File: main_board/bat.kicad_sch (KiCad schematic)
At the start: 44 parts, among them IC1 MP2722GRH-0000-Z, IC2 MP3429GL-Z, IC3 NX3DV42GU, IC4 AP2204R-3.3TRG1, J4 USB_B_Micro, J5 USB_C_Receptacle_USB2.0, U3 ATmega32U4-M, Y1 Crystal

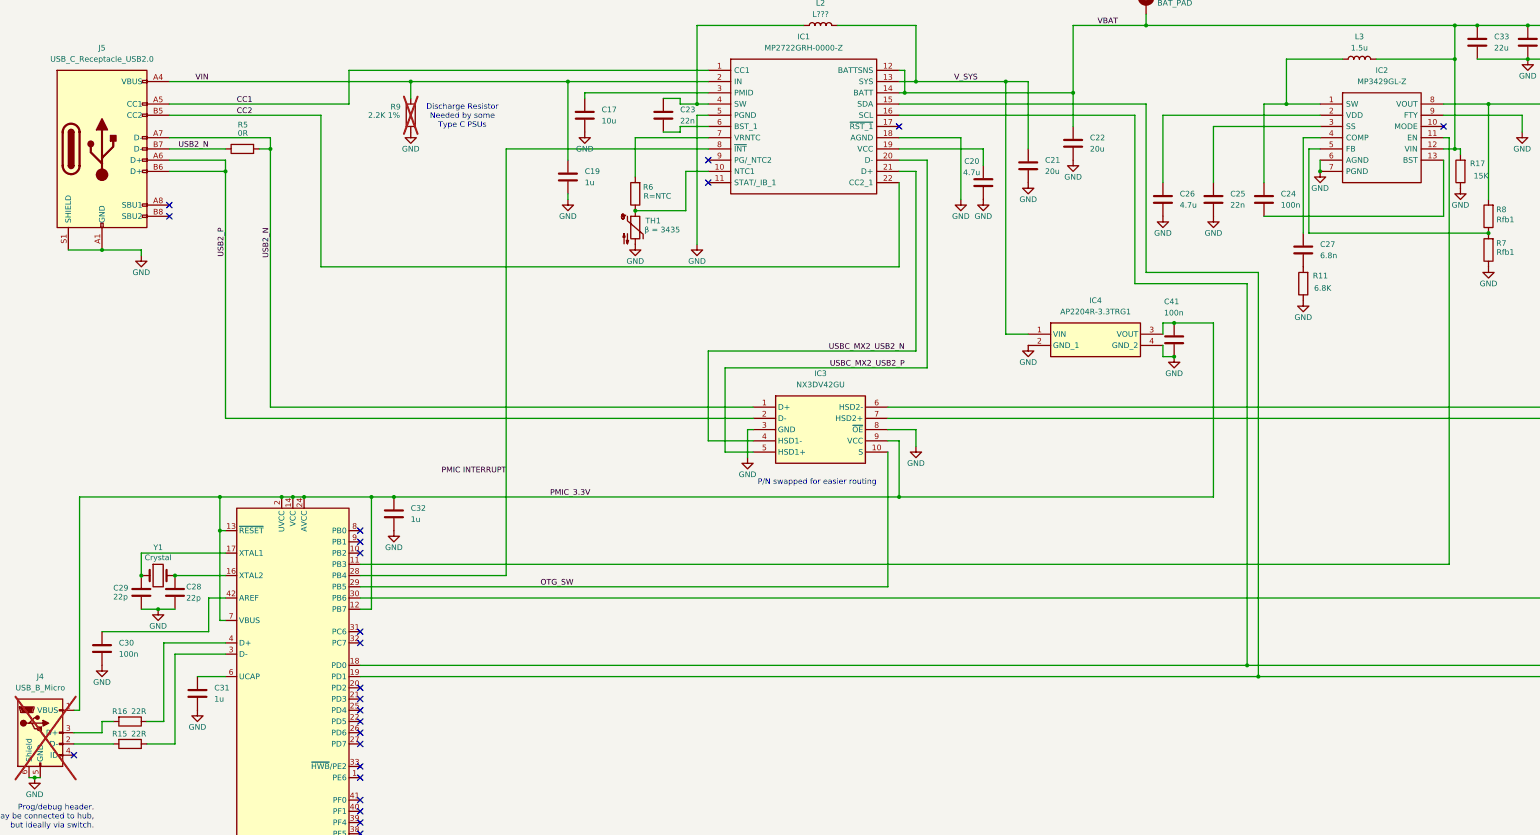
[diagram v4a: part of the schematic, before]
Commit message: Bunch more routing, mainly added MIPI interface, reworked power management a bit
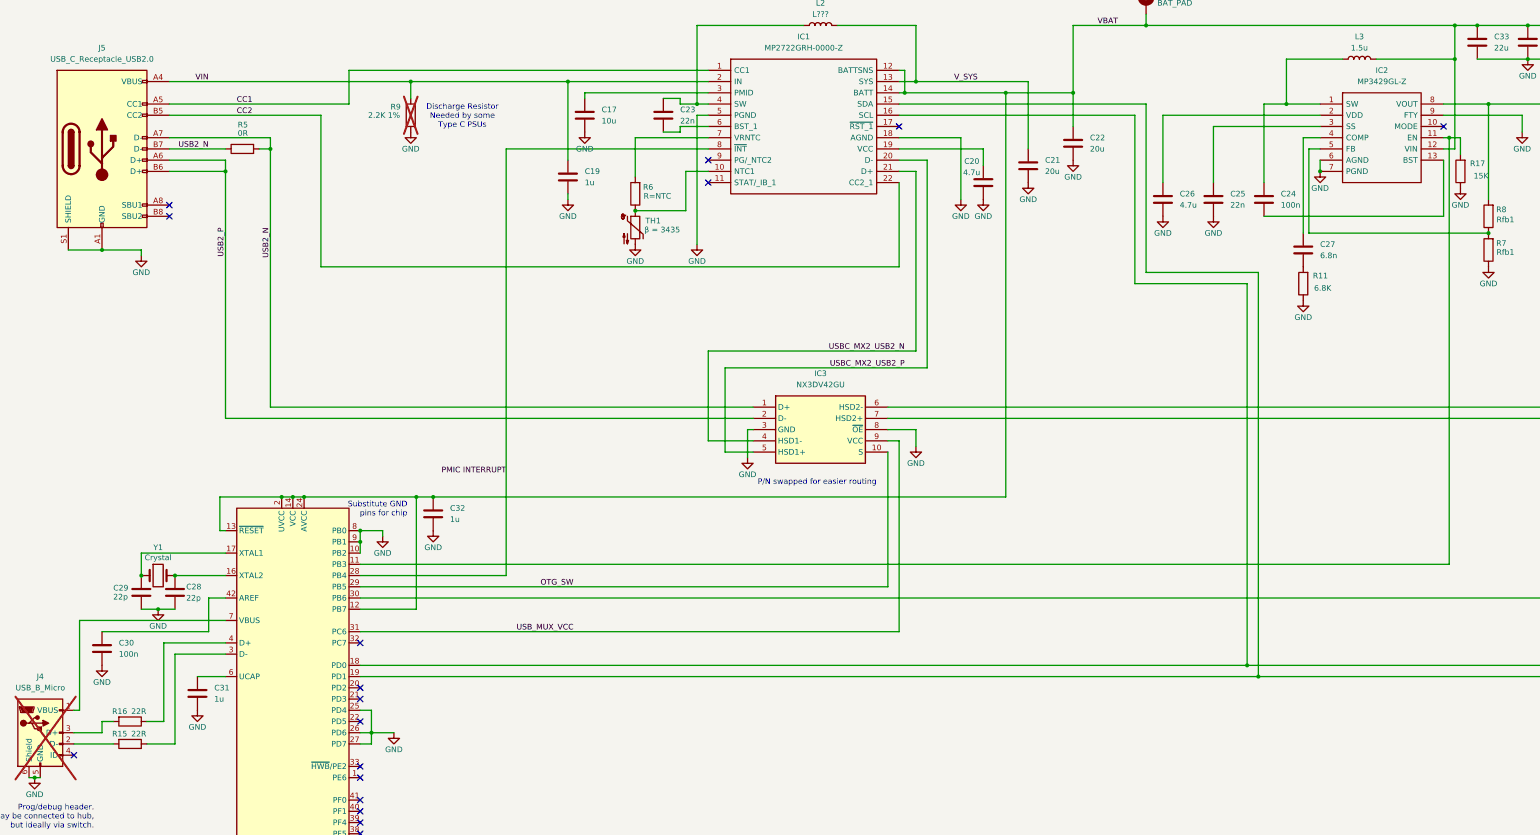
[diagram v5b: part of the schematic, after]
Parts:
- removed C41: 100n, Capacitor_SMD:C_0805_2012Metric_Pad1.18x1.45mm_HandSolder, symbol Device:C
- removed IC4: AP2204R-3.3TRG1, AP2204R33TRG1, symbol 000_Custom:AP2204R-3.3TRG1
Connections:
- net GND: now also U3.10 (PB2), U3.25 (PD4), U3.26 (PD6), U3.27 (PD7), U3.8 (PB0), U3.9 (PB1)
- net VBAT: now also C32.2, U3.12 (PB7), U3.13 (~{RESET}), U3.14 (VCC), U3.2 (UVCC), U3.24 (AVCC), U3.34 (VCC), U3.44 (AVCC); no longer R17.2
- net at IC2.11 (EN), U3.11 (PB3): now also R17.2
- net USB_MUX_VCC: now reaches U3.31 (PC6)
- net USB_MUX_VCC: now also IC3.9 (VCC)
- removed net PMIC_3.3V: C32.2, IC3.9 (VCC), J4.1 (VBUS), U3.12 (PB7), U3.13 (~{RESET}), U3.14 (VCC), U3.2 (UVCC), U3.24 (AVCC), U3.34 (VCC), U3.44 (AVCC), U3.7 (VBUS)
- new net: J4.1 (VBUS), U3.7 (VBUS)
- no-connect marks 26 -> 19
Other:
- note added: "Substitute GND pins for chip"
- moved on the sheet: C32

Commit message: Bunch of fixes + audio out interface
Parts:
- added C41: 100n, Capacitor_SMD:C_0805_2012Metric_Pad1.18x1.45mm_HandSolder, symbol Device:C
- added R26: 430K, Resistor_SMD:R_0805_2012Metric_Pad1.20x1.40mm_HandSolder, symbol Device:R
- added U5: AP2204RB-3.3, Package_TO_SOT_SMD:SOT-89-3, symbol Regulator_Linear:AP2204RB-3.3
- C20, C26: value 4.7u -> 10u
- C25: value 22n -> 100n
- C27: value 6.8n -> 10n
- C30: value 100n -> 1u
- L2: value L??? -> 4.7u
- R7: value Rfb1 -> 100K
- R8: value Rfb1 -> 33K
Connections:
- net +5V: now also R26.2; no longer R8.2
- net GND: now also U3.11 (PB3), U3.12 (PB7), C41.1, U5.2 (GND)
- net VBAT: no longer C32.2, U3.12 (PB7), U3.13 (~{RESET}), U3.14 (VCC), U3.2 (UVCC), U3.24 (AVCC), U3.34 (VCC), U3.44 (AVCC)
- net V_SYS: now also U5.3 (VIN)
- net BOOST_EN: now reaches IC2.11 (EN), R17.2
- net BOOST_EN: now also U3.1 (PE6); no longer U3.11 (PB3)
- net at J4.1 (VBUS), U3.7 (VBUS): now also U3.2 (UVCC)
- net 3.3v: now reaches U3.41 (PF0)
- net CM5_PMIC_EN renamed USB_SW_VCC
- net USB_SW_VCC: now also IC3.9 (VCC)
- net USB_MUX_VCC: no longer names the net of U3.31 (PC6)
- net USB_MUX_VCC: no longer IC3.9 (VCC)
- new net: R26.1, R8.2
- new net PMIC_3.3V: C32.2, C41.2, U3.13 (~{RESET}), U3.14 (VCC), U3.24 (AVCC), U3.34 (VCC), U3.44 (AVCC), U5.1 (VOUT)
- no-connect marks 19 -> 7

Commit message: Implement power monitoring
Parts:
- removed H9: BAT_PAD, TestPoint:TestPoint_Pad_4.0x4.0mm, symbol Mechanical:MountingHole_Pad_MP
- added BT1: Battery_Cell, 000_custom:Bat_terminal, symbol Device:Battery_Cell
- added C64: 100n, Capacitor_SMD:C_0805_2012Metric_Pad1.18x1.45mm_HandSolder, symbol Device:C
- added R41: 0.01R, Resistor_SMD:R_1206_3216Metric_Pad1.30x1.75mm_HandSolder, symbol Device:R
- added R42, R43: 10R, Resistor_SMD:R_0805_2012Metric_Pad1.20x1.40mm_HandSolder, symbol Device:R
- added U7: INA220AIDGST, DGS10, symbol 000_Custom:INA220AIDGST
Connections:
- net GND: now also BT1.2 (-), U7.1 (A1), U7.2 (A0), U7.7 (GND)
- net IIC_SCL: now also U7.5 (SCL)
- net IIC_SDA: now also U7.4 (SDA)
- net PMIC_3.3V: now also U7.6 (VS)
- net VBAT: now also R41.2, R43.2, U7.8 (VBUS)
- new net: BT1.1 (+), R41.1, R42.2
- new net: C64.1, R42.1, U7.9 (VIN-)
- new net: C64.2, R43.1, U7.10 (VIN+)
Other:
- moved on the sheet: C17, C19, C20, C21, C22, C23, C24, C25, C26, C27, C28, C29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

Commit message: Add expansion slot
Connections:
- net GND: no longer U7.1 (A1), U7.2 (A0)
- net IIC_SDA: now also U7.1 (A1), U7.2 (A0)
- net USBC_MX2_USB2_N: now also IC1.20 (D-), IC3.5 (HSD1+); no longer IC1.21 (D+), IC3.4 (HSD1-)
- net USBC_MX2_USB2_P: now also IC1.21 (D+), IC3.4 (HSD1-); no longer IC1.20 (D-), IC3.5 (HSD1+)
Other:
- moved on the sheet: R43
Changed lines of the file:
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@@
 	)
 	(junction
-		(at 358.14 54.61)
-		(diameter 0)
-		(color 0 0 0 0)
-	)
-	(junction
 		(at 163.83 115.57)
 		(diameter 0)
@@
 	)
 	(junction
+		(at 262.89 57.15)
+		(diameter 0)
+		(color 0 0 0 0)
+	)
+	(junction
 		(at 262.89 49.53)
 		(diameter 0)
@@
 	)
 	(junction
+		(at 358.14 52.07)
+		(diameter 0)
+		(color 0 0 0 0)
+	)
+	(junction
 		(at 227.33 86.36)
 		(diameter 0)
@@
 	)
 	(junction
-		(at 262.89 55.88)
+		(at 361.95 46.99)
 		(diameter 0)
 		(color 0 0 0 0)
@@
 	(wire
 		(pts
-			(xy 284.48 55.88) (xy 284.48 54.61)
-		)
-		(stroke
-			(width 0)
-			(type default)
-		)
-	)
-	(wire
-		(pts
 			(xy 318.77 99.06) (xy 314.96 99.06)
 		)
@@
 	(wire
 		(pts
-			(xy 262.89 55.88) (xy 267.97 55.88)
+			(xy 262.89 57.15) (xy 269.24 57.15)
 		)
 		(stroke
@@
 	(wire
 		(pts
+			(xy 262.89 49.53) (xy 262.89 57.15)
+		)
+		(stroke
+			(width 0)
+			(type default)
+		)
+	)
+	(wire
+		(pts
 			(xy 58.42 86.36) (xy 113.03 86.36)
 		)
@@
 	(wire
 		(pts
+			(xy 361.95 52.07) (xy 361.95 46.99)
+		)
+		(stroke
+			(width 0)
+			(type default)
+		)
+	)
+	(wire
+		(pts
 			(xy 284.48 29.21) (xy 274.32 29.21)
 		)
@@
 	(wire
 		(pts
-			(xy 220.98 160.02) (xy 381 160.02)
+			(xy 358.14 52.07) (xy 358.14 54.61)
 		)
 		(stroke
@@
 	(wire
 		(pts
-			(xy 86.36 180.34) (xy 88.9 180.34)
+			(xy 220.98 160.02) (xy 381 160.02)
 		)
 		(stroke
@@
 	(wire
 		(pts
-			(xy 43.18 231.14) (xy 45.72 231.14)
+			(xy 86.36 180.34) (xy 88.9 180.34)
 		)
 		(stroke
@@
 	(wire
 		(pts
-			(xy 314.96 99.06) (xy 314.96 120.65)
+			(xy 43.18 231.14) (xy 45.72 231.14)
 		)
 		(stroke
@@
 	(wire
 		(pts
-			(xy 101.6 203.2) (xy 224.79 203.2)
+			(xy 314.96 99.06) (xy 314.96 120.65)
 		)
 		(stroke
@@
 	(wire
 		(pts
-			(xy 134.62 101.6) (xy 134.62 198.12)
+			(xy 101.6 203.2) (xy 224.79 203.2)
 		)
 		(stroke
@@
 	(wire
 		(pts
-			(xy 358.14 54.61) (xy 358.14 58.42)
+			(xy 134.62 101.6) (xy 134.62 198.12)
 		)
 		(stroke
@@
 	(wire
 		(pts
+			(xy 361.95 46.99) (xy 403.86 46.99)
+		)
+		(stroke
+			(width 0)
+			(type default)
+		)
+	)
+	(wire
+		(pts
 			(xy 372.11 106.68) (xy 378.46 106.68)
 		)
@@
 	(wire
 		(pts
+			(xy 284.48 57.15) (xy 284.48 54.61)
+		)
+		(stroke
+			(width 0)
+			(type default)
+		)
+	)
+	(wire
+		(pts
 			(xy 36.83 228.6) (xy 38.1 228.6)
 		)
@@
 	(wire
 		(pts
-			(xy 262.89 49.53) (xy 262.89 55.88)
-		)
-		(stroke
-			(width 0)
-			(type default)
-		)
-	)
-	(wire
-		(pts
 			(xy 101.6 187.96) (xy 101.6 190.5)
 		)
@@
 	(wire
 		(pts
-			(xy 275.59 55.88) (xy 284.48 55.88)
+			(xy 276.86 57.15) (xy 284.48 57.15)
 		)
 		(stroke
@@
 	(wire
 		(pts
-			(xy 262.89 55.88) (xy 262.89 73.66)
-		)
-		(stroke
-			(width 0)
-			(type default)
-		)
-	)
-	(wire
-		(pts
 			(xy 209.55 73.66) (xy 227.33 73.66)
 		)
@@
 	(wire
 		(pts
-			(xy 358.14 52.07) (xy 358.14 54.61)
-		)
-		(stroke
-			(width 0)
-			(type default)
-		)
-	)
-	(wire
-		(pts
 			(xy 43.18 124.46) (xy 52.07 124.46)
 		)
@@
 	(wire
 		(pts
-			(xy 358.14 46.99) (xy 403.86 46.99)
+			(xy 358.14 46.99) (xy 361.95 46.99)
 		)
 		(stroke
@@
 	(wire
 		(pts
+			(xy 262.89 57.15) (xy 262.89 73.66)
+		)
+		(stroke
+			(width 0)
+			(type default)
+		)
+	)
+	(wire
+		(pts
 			(xy 284.48 54.61) (xy 323.85 54.61)
 		)
@@
 	(wire
 		(pts
+			(xy 358.14 52.07) (xy 361.95 52.07)
+		)
+		(stroke
+			(width 0)
+			(type default)
+		)
+	)
+	(wire
+		(pts
 			(xy 78.74 101.6) (xy 81.28 101.6)
 		)
@@
 	(text "P/N swapped for easier routing"
 		(exclude_from_sim no)
-		(at 218.44 177.8 0)
+		(at 224.536 143.002 0)
 		(effects
 			(font
@@
 		)
 	)
-	(label "PMIC INTERRUPT"
-		(at 134.62 175.26 180)
+	(label "USBC_MX2_USB2_N"
+		(at 219.71 151.13 180)
 		(fields_autoplaced yes)
 		(effects
@@
 		)
 	)
-	(label "USB2_P"
-		(at 71.12 119.38 270)
+	(label "PMIC INTERRUPT"
+		(at 134.62 175.26 180)
 		(fields_autoplaced yes)
 		(effects
@@
 		)
 	)
-	(label "CC2"
-		(at 73.66 93.98 0)
+	(label "USB2_P"
+		(at 71.12 119.38 270)
 		(fields_autoplaced yes)
 		(effects
@@
 				(size 1.27 1.27)
 			)
-			(justify left bottom)
+			(justify right bottom)
 		)
 	)
-	(label "USBC_MX2_USB2_N"
-		(at 224.79 147.32 180)
+	(label "CC2"
+		(at 73.66 93.98 0)
 		(fields_autoplaced yes)
 		(effects
@@
 				(size 1.27 1.27)
 			)
-			(justify right bottom)
+			(justify left bottom)
 		)
 	)
@@
 	)
 	(label "USBC_MX2_USB2_P"
-		(at 224.79 151.13 180)
+		(at 219.71 147.32 180)
 		(fields_autoplaced yes)
 		(effects
@@
 	(symbol
 		(lib_id "power:GND")
-		(at 358.14 58.42 0)
-		(unit 1)
-		(exclude_from_sim no)
-		(in_bom yes)
-		(on_board yes)
-		(dnp no)
-		(property "Reference" "#PWR087"
-			(at 358.14 64.77 0)
-			(effects
-				(font
-					(size 1.27 1.27)
-				)
-				(hide yes)
-			)
-		)
-		(property "Value" "GND"
-			(at 358.14 62.23 0)
-			(effects
-				(font
-					(size 1.27 1.27)
-				)
-			)
-		)
-		(property "Footprint" ""
-			(at 358.14 58.42 0)
-			(effects
-				(font
-					(size 1.27 1.27)
-				)
-				(hide yes)
-			)
-		)
-		(property "Datasheet" ""
-			(at 358.14 58.42 0)
-			(effects
-				(font
-					(size 1.27 1.27)
-				)
-				(hide yes)
-			)
-		)
-		(property "Description" "Power symbol creates a global label with name \"GND\" , ground"
-			(at 358.14 58.42 0)
-			(effects
-				(font
-					(size 1.27 1.27)
-				)
-				(hide yes)
-			)
-		)
-		(pin "1"
-		)
-		(instances
-			(project "main_board"
-				(path "/e63e39d7-6ac0-4ffd-8aa3-1841a4541b55/b84f1a66-243e-4389-abcf-18bc380f8da3"
-					(reference "#PWR087")
-					(unit 1)
-				)
-			)
-		)
-	)
-	(symbol
-		(lib_id "power:GND")
 		(at 118.11 187.96 0)
 		(unit 1)
@@
 	(symbol
 		(lib_id "Device:R")
-		(at 271.78 55.88 270)
+		(at 273.05 57.15 270)
 		(unit 1)
 		(exclude_from_sim no)
@@
 		(dnp no)
 		(property "Reference" "R43"
-			(at 269.748 51.308 90)
+			(at 271.018 52.578 90)
 			(effects
 				(font
@@
 		)
 		(property "Value" "10R"
-			(at 269.494 53.34 90)
+			(at 270.764 54.61 90)
 			(effects
 				(font
@@
 		)
 		(property "Footprint" "Resistor_SMD:R_0805_2012Metric_Pad1.20x1.40mm_HandSolder"
-			(at 271.78 54.102 90)
+			(at 273.05 55.372 90)
 			(effects
 				(font
@@
 		)
 		(property "Datasheet" "https://fscdn.rohm.com/en/products/databook/datasheet/passive/resistor/chip_resistor/mcr-e.pdf"
-			(at 271.78 55.88 0)
+			(at 273.05 57.15 0)
 			(effects
 				(font
@@
 		)
 		(property "Description" ""
-			(at 271.78 55.88 0)
+			(at 273.05 57.15 0)
 			(effects
 				(font
@@
 		)
 		(property "Field4" "Farnell"
-			(at 271.78 55.88 0)
+			(at 273.05 57.15 0)
 			(effects
 				(font
@@
 		)
 		(property "Field5" ""
-			(at 271.78 55.88 0)
+			(at 273.05 57.15 0)
 			(effects
 				(font
@@
 		)
 		(property "Field7" "Rohm"
-			(at 271.78 55.88 0)
+			(at 273.05 57.15 0)
 			(effects
 				(font
@@
 		)
 		(property "Field6" "MCR01MZPF1002"
-			(at 271.78 55.88 0)
+			(at 273.05 57.15 0)
 			(effects
 				(font
@@
 		)
 		(property "Part Description" "Resistor 10K M1005 1% 63mW"
-			(at 271.78 55.88 0)
+			(at 273.05 57.15 0)
 			(effects
 				(font
